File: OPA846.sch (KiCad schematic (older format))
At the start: 9 parts, among them J1 Conn_Coaxial, U6 OPA846

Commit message: Changed inverter IC, added some decoupling
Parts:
- removed R11: 51R, Resistor_SMD:R_0402_1005Metric, symbol Device:R_US
- added C25, C26, C27: 1u, Capacitor_SMD:C_0402_1005Metric, symbol Device:C
- added C28, C29: 0u1, Capacitor_SMD:C_0402_1005Metric, symbol Device:C
- R8, R9: value 51R -> 49R9
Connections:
- net +5V: now also C26.2, C28.1
- net -5V: now also C27.1, C29.2
- net GND: now also C26.1, C27.2, C28.2, C29.1
- net Signal: now also C25.1
- net at R10.1, U6.1: now also C25.2

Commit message: Finsihed layout for 1v2
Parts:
- removed C26, C27: 1u, Capacitor_SMD:C_0402_1005Metric, symbol Device:C
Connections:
- net -5V renamed -4V
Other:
- note added: "Amplifier"
- note added: "Decoupling"
- moved on the sheet: C13, C14, C50, C53, C54, J6, R32, R33, R34, R35, U11

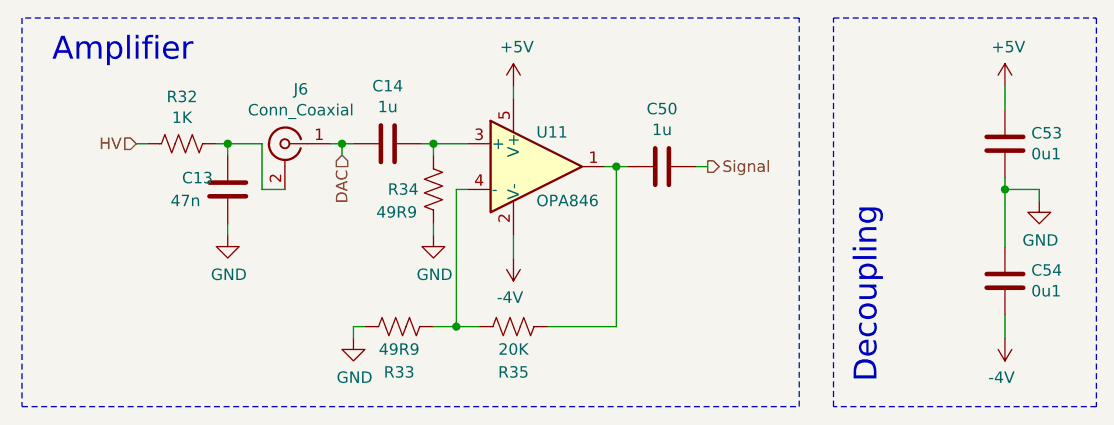
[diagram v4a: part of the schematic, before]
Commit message: Added more decopling, changed I2C jack to be compatible with 6P4C
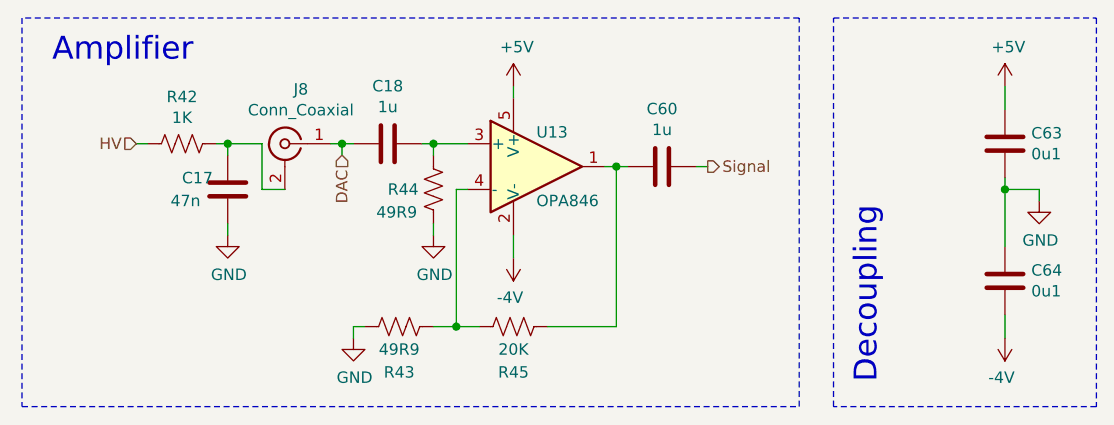
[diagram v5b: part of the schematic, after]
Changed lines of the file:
@@
 AR Path="/5C2275FC/5C221C17" Ref="U12"  Part="1"
 AR Path="/5C227601/5C221C17" Ref="U13"  Part="1"
-F 0 "U11" H 2800 1350 50  0000 L CNN
+F 0 "U13" H 2800 1350 50  0000 L CNN
 F 1 "OPA846" H 2800 1050 50  0000 L CNN
 F 2 "Package_TO_SOT_SMD:SOT-23-5" H 2700 1200 50  0001 C CNN
@@
 AR Path="/5C2275FC/5C221C68" Ref="#PWR050"  Part="1"
 AR Path="/5C227601/5C221C68" Ref="#PWR055"  Part="1"
-F 0 "#PWR045" H 2700 700 50  0001 C CNN
+F 0 "#PWR055" H 2700 700 50  0001 C CNN
 F 1 "+5V" H 2715 1023 50  0000 C CNN
 F 2 "" H 2700 850 50  0001 C CNN
@@
 AR Path="/5C2275FC/5C221E33" Ref="R40"  Part="1"
 AR Path="/5C227601/5C221E33" Ref="R45"  Part="1"
-F 0 "R35" V 2900 1900 50  0000 C CNN
+F 0 "R45" V 2900 1900 50  0000 C CNN
 F 1 "20K" V 2800 1900 50  0000 C CNN
 F 2 "Resistor_SMD:R_0402_1005Metric" V 2740 1890 50  0001 C CNN
@@
 AR Path="/5C2275FC/5C221F1E" Ref="R38"  Part="1"
 AR Path="/5C227601/5C221F1E" Ref="R43"  Part="1"
-F 0 "R33" V 2000 1900 50  0000 C CNN
+F 0 "R43" V 2000 1900 50  0000 C CNN
 F 1 "49R9" V 2100 1900 50  0000 C CNN
 F 2 "Resistor_SMD:R_0402_1005Metric" V 2240 1890 50  0001 C CNN
@@
 AR Path="/5C2275FC/5C221F9E" Ref="#PWR048"  Part="1"
 AR Path="/5C227601/5C221F9E" Ref="#PWR053"  Part="1"
-F 0 "#PWR043" H 2000 1700 50  0001 C CNN
+F 0 "#PWR053" H 2000 1700 50  0001 C CNN
 F 1 "GND" H 2005 1777 50  0000 C CNN
 F 2 "" H 2000 1950 50  0001 C CNN
@@
 AR Path="/5C2275FC/5C222395" Ref="#PWR049"  Part="1"
 AR Path="/5C227601/5C222395" Ref="#PWR054"  Part="1"
-F 0 "#PWR044" H 2350 1250 50  0001 C CNN
+F 0 "#PWR054" H 2350 1250 50  0001 C CNN
 F 1 "GND" H 2355 1327 50  0000 C CNN
 F 2 "" H 2350 1500 50  0001 C CNN
@@
 AR Path="/5C2275FC/5C2223CB" Ref="R39"  Part="1"
 AR Path="/5C227601/5C2223CB" Ref="R44"  Part="1"
-F 0 "R34" H 2550 1300 50  0000 R CNN
+F 0 "R44" H 2550 1300 50  0000 R CNN
 F 1 "49R9" H 2600 1400 50  0000 R CNN
 F 2 "Resistor_SMD:R_0402_1005Metric" V 2390 1290 50  0001 C CNN
@@
 AR Path="/5C2275FC/5C223897" Ref="J7"  Part="1"
 AR Path="/5C227601/5C223897" Ref="J8"  Part="1"
-F 0 "J6" H 1630 1338 50  0000 C CNN
+F 0 "J8" H 1630 1338 50  0000 C CNN
 F 1 "Conn_Coaxial" H 1630 1247 50  0000 C CNN
 F 2 "Connector_Coaxial:U.FL_Hirose_U.FL-R-SMT-1_Vertical" H 1700 1100 50  0001 C CNN
@@
 AR Path="/5C2275FC/5C224FDA" Ref="R37"  Part="1"
 AR Path="/5C227601/5C224FDA" Ref="R42"  Part="1"
-F 0 "R32" V 1045 1100 50  0000 C CNN
+F 0 "R42" V 1045 1100 50  0000 C CNN
 F 1 "1K" V 1136 1100 50  0000 C CNN
 F 2 "Resistor_SMD:R_0402_1005Metric" V 1290 1090 50  0001 C CNN
@@
 AR Path="/5C2275FC/5C225760" Ref="#PWR047"  Part="1"
 AR Path="/5C227601/5C225760" Ref="#PWR052"  Part="1"
-F 0 "#PWR042" H 1450 1250 50  0001 C CNN
+F 0 "#PWR052" H 1450 1250 50  0001 C CNN
 F 1 "GND" H 1455 1327 50  0000 C CNN
 F 2 "" H 1450 1500 50  0001 C CNN
@@
 AR Path="/5C2275FC/5C2261DF" Ref="C16"  Part="1"
 AR Path="/5C227601/5C2261DF" Ref="C18"  Part="1"
-F 0 "C14" V 1898 1100 50  0000 C CNN
+F 0 "C18" V 1898 1100 50  0000 C CNN
 F 1 "1u" V 1989 1100 50  0000 C CNN
 F 2 "Capacitor_SMD:C_0402_1005Metric" H 2188 950 50  0001 C CNN
@@
 AR Path="/5C2275FC/5C225702" Ref="C15"  Part="1"
 AR Path="/5C227601/5C225702" Ref="C17"  Part="1"
-F 0 "C13" H 1250 1350 50  0000 L CNN
+F 0 "C17" H 1250 1350 50  0000 L CNN
 F 1 "47n" H 1200 1250 50  0000 L CNN
 F 2 "Capacitor_SMD:C_0402_1005Metric" H 1488 1150 50  0001 C CNN
@@
 AR Path="/5C2275FC/5D85554C" Ref="C55"  Part="1"
 AR Path="/5C227601/5D85554C" Ref="C60"  Part="1"
-F 0 "C50" V 3098 1200 50  0000 C CNN
+F 0 "C60" V 3098 1200 50  0000 C CNN
 F 1 "1u" V 3189 1200 50  0000 C CNN
 F 2 "Capacitor_SMD:C_0402_1005Metric" H 3388 1050 50  0001 C CNN
@@
 AR Path="/5C2275FC/5D862B10" Ref="#PWR072"  Part="1"
 AR Path="/5C227601/5D862B10" Ref="#PWR075"  Part="1"
-F 0 "#PWR069" H 4850 700 50  0001 C CNN
+F 0 "#PWR075" H 4850 700 50  0001 C CNN
 F 1 "+5V" H 4865 1023 50  0000 C CNN
 F 2 "" H 4850 850 50  0001 C CNN
@@
 AR Path="/5C2275FC/5D85DAAD" Ref="C59"  Part="1"
 AR Path="/5C227601/5D85DAAD" Ref="C64"  Part="1"
-F 0 "C54" H 4965 1746 50  0000 L CNN
+F 0 "C64" H 4965 1746 50  0000 L CNN
 F 1 "0u1" H 4965 1655 50  0000 L CNN
 F 2 "Capacitor_SMD:C_0402_1005Metric" H 4888 1550 50  0001 C CNN
@@
 AR Path="/5C2275FC/5D856631" Ref="#PWR074"  Part="1"
 AR Path="/5C227601/5D856631" Ref="#PWR077"  Part="1"
-F 0 "#PWR071" H 5000 1100 50  0001 C CNN
+F 0 "#PWR077" H 5000 1100 50  0001 C CNN
 F 1 "GND" H 5005 1177 50  0000 C CNN
 F 2 "" H 5000 1350 50  0001 C CNN
@@
 AR Path="/5C2275FC/5D85479D" Ref="C58"  Part="1"
 AR Path="/5C227601/5D85479D" Ref="C63"  Part="1"
-F 0 "C53" H 4965 1146 50  0000 L CNN
+F 0 "C63" H 4965 1146 50  0000 L CNN
 F 1 "0u1" H 4965 1055 50  0000 L CNN
 F 2 "Capacitor_SMD:C_0402_1005Metric" H 4888 950 50  0001 C CNN
@@
 AR Path="/5C2275F2/5E52130F" Ref="#PWR0133"  Part="1"
 AR Path="/5C2275F7/5E52130F" Ref="#PWR0135"  Part="1"
-F 0 "#PWR0135" H 2700 1450 50  0001 C CNN
+F 0 "#PWR0139" H 2700 1450 50  0001 C CNN
 F 1 "-4V" H 2715 1773 50  0000 C CNN
 F 2 "" H 2700 1600 50  0001 C CNN
@@
 AR Path="/5C2275F2/5E52333A" Ref="#PWR0134"  Part="1"
 AR Path="/5C2275F7/5E52333A" Ref="#PWR0136"  Part="1"
-F 0 "#PWR0136" H 4850 1800 50  0001 C CNN
+F 0 "#PWR0140" H 4850 1800 50  0001 C CNN
 F 1 "-4V" H 4865 2123 50  0000 C CNN
 F 2 "" H 4850 1950 50  0001 C CNN
